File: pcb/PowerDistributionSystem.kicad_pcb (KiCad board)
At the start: 4 copper layers, 66 x 60 mm, 65 parts, among them J1 S04B-PASK-2, J2 S04B-PASK-2, J3 S04B-PASK-2, J4 S04B-PASK-2, J5 S04B-PASK-2, J8 S04B-PASK-2, U1 TPS22810DRV, U2 D24V7F5, U3 D24V7F3, U4 TMC2209-LA-T, U5 TMC2209-LA-T, U6 TMC2209-LA-T

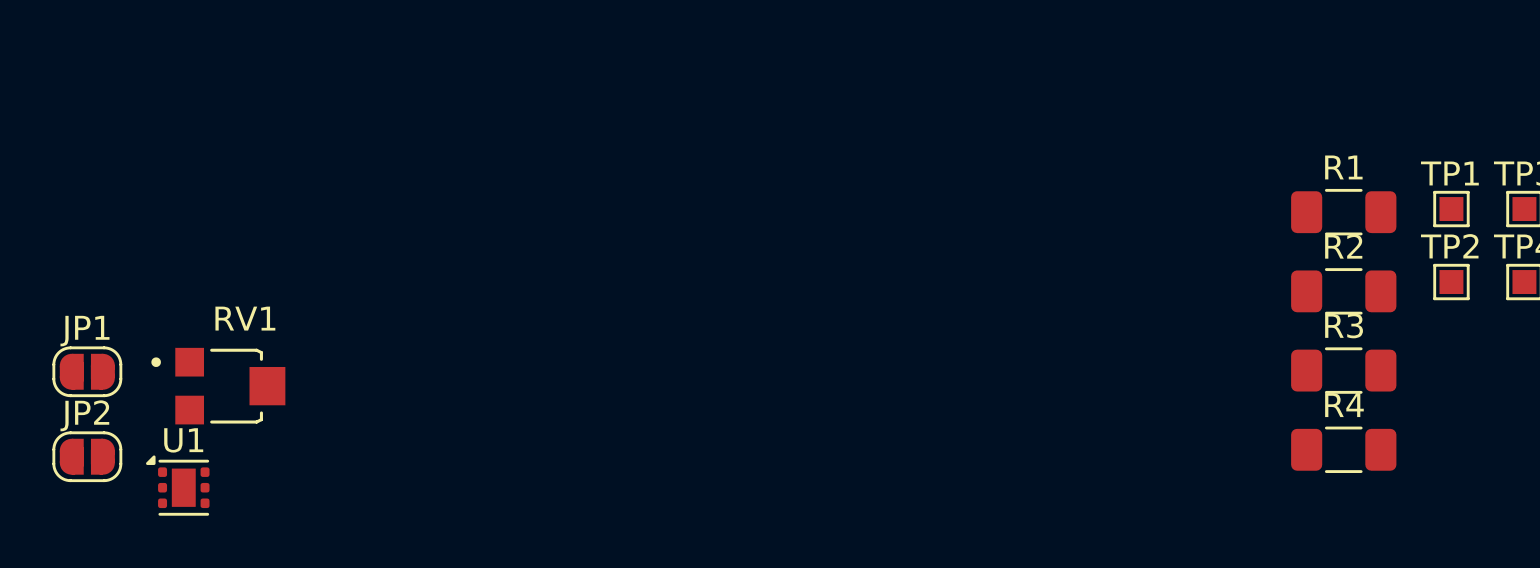
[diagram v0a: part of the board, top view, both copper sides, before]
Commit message: Removed potentiometer for VREF.
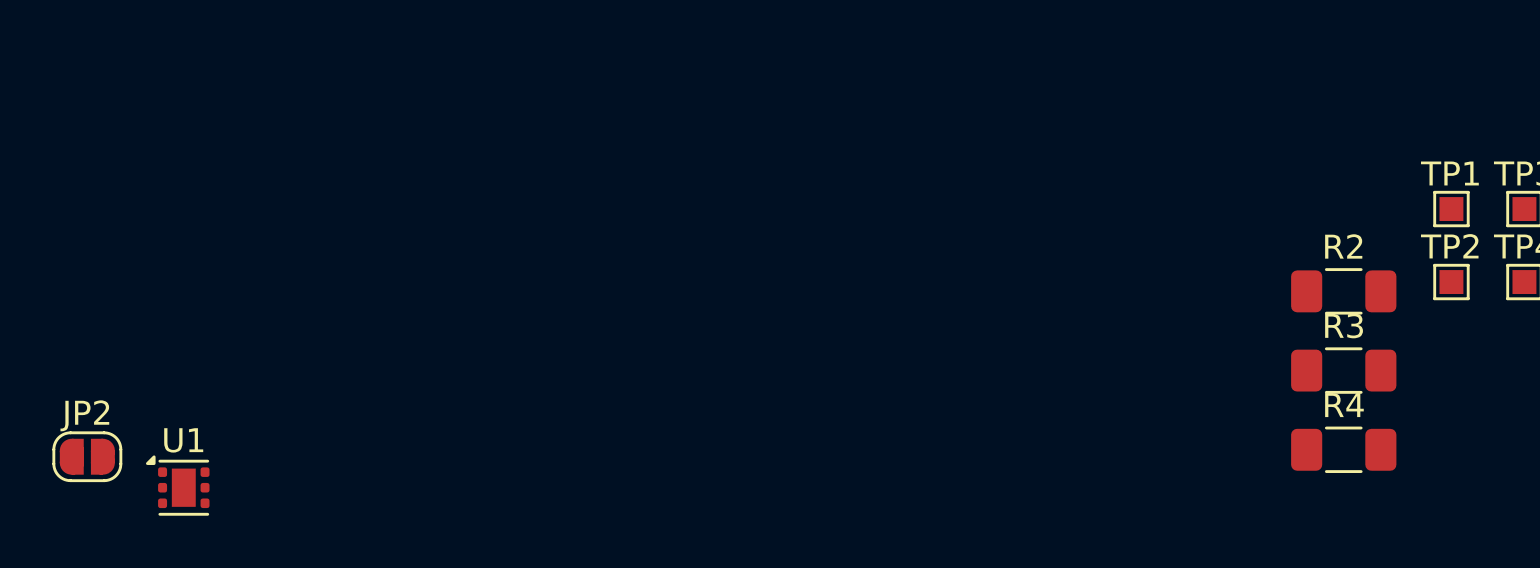
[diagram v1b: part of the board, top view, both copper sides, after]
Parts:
- removed JP1: SolderJumper_2_Open, Jumper:SolderJumper-2_P1.3mm_Open_RoundedPad1.0x1.5mm
- removed R1: 33k, Resistor_SMD:R_1206_3216Metric_Pad1.30x1.75mm_HandSolder
- removed RV1: 10k, pcb:TRIM_35WR10KLFTR

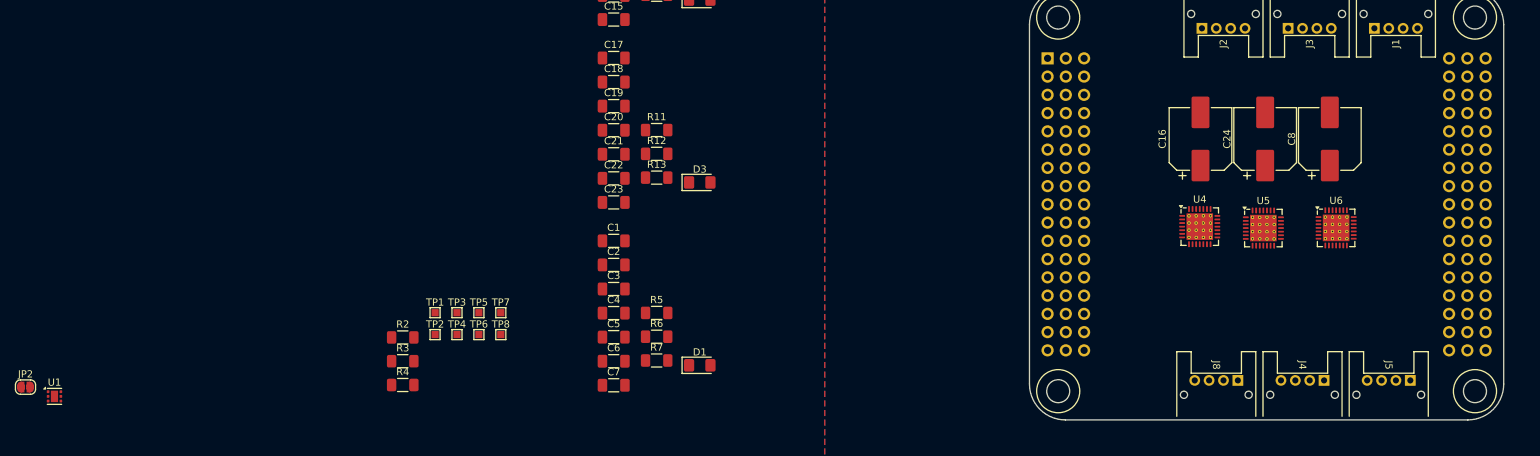
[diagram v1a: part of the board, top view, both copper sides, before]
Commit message: Updated footprints for stack connector's new asymmetry.
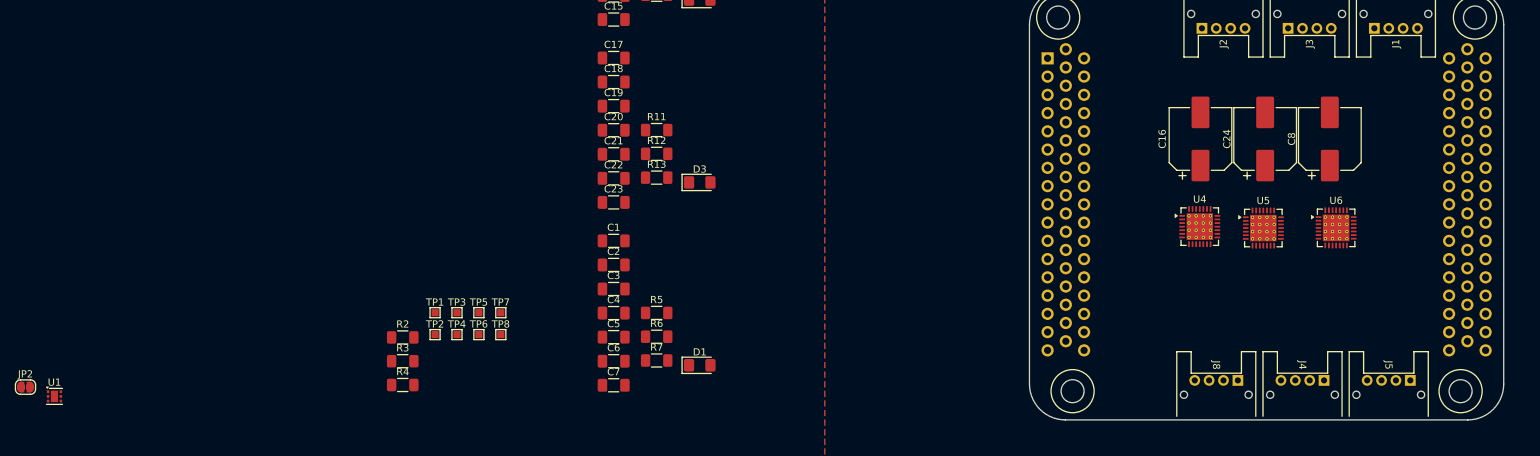
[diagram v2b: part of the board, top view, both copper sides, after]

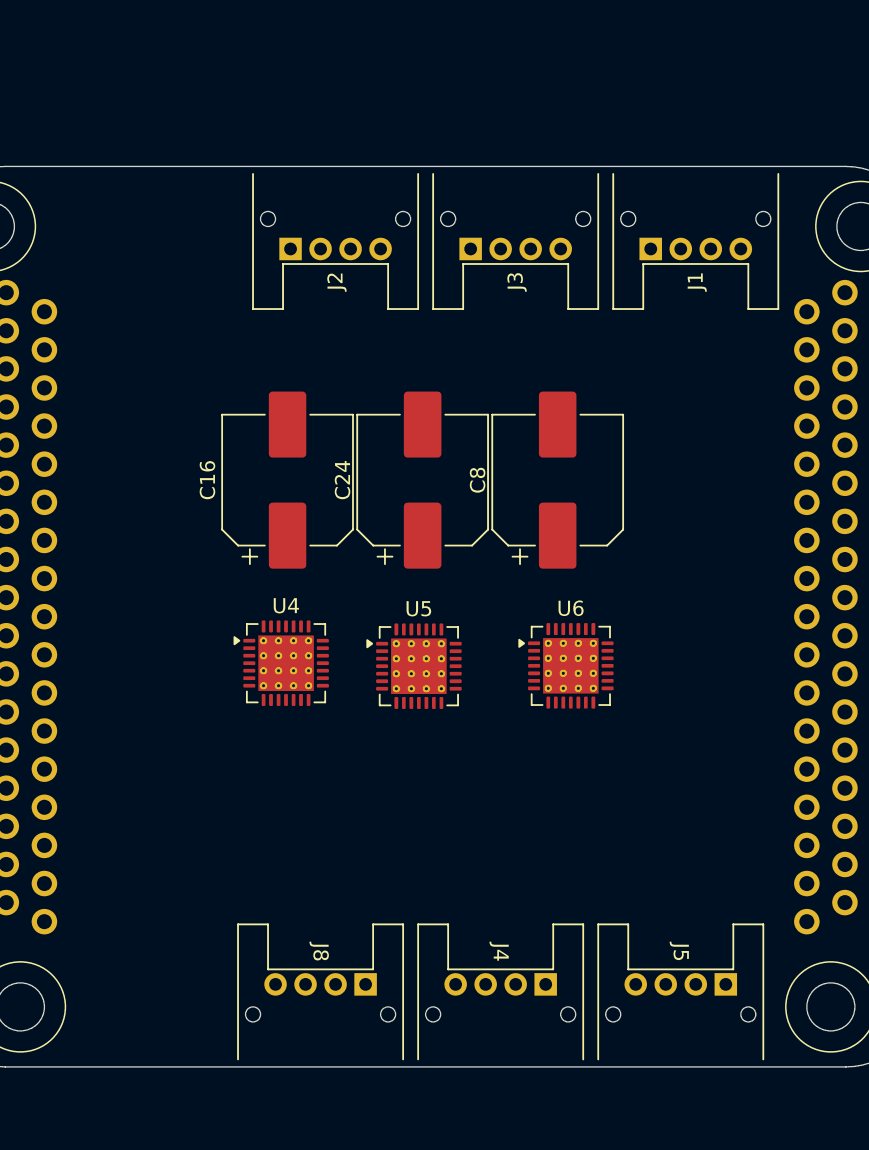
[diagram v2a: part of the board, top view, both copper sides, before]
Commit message: Instead of S04B-PASK-2 connectors, regular 2.54mm horizontal pin headers will be used.
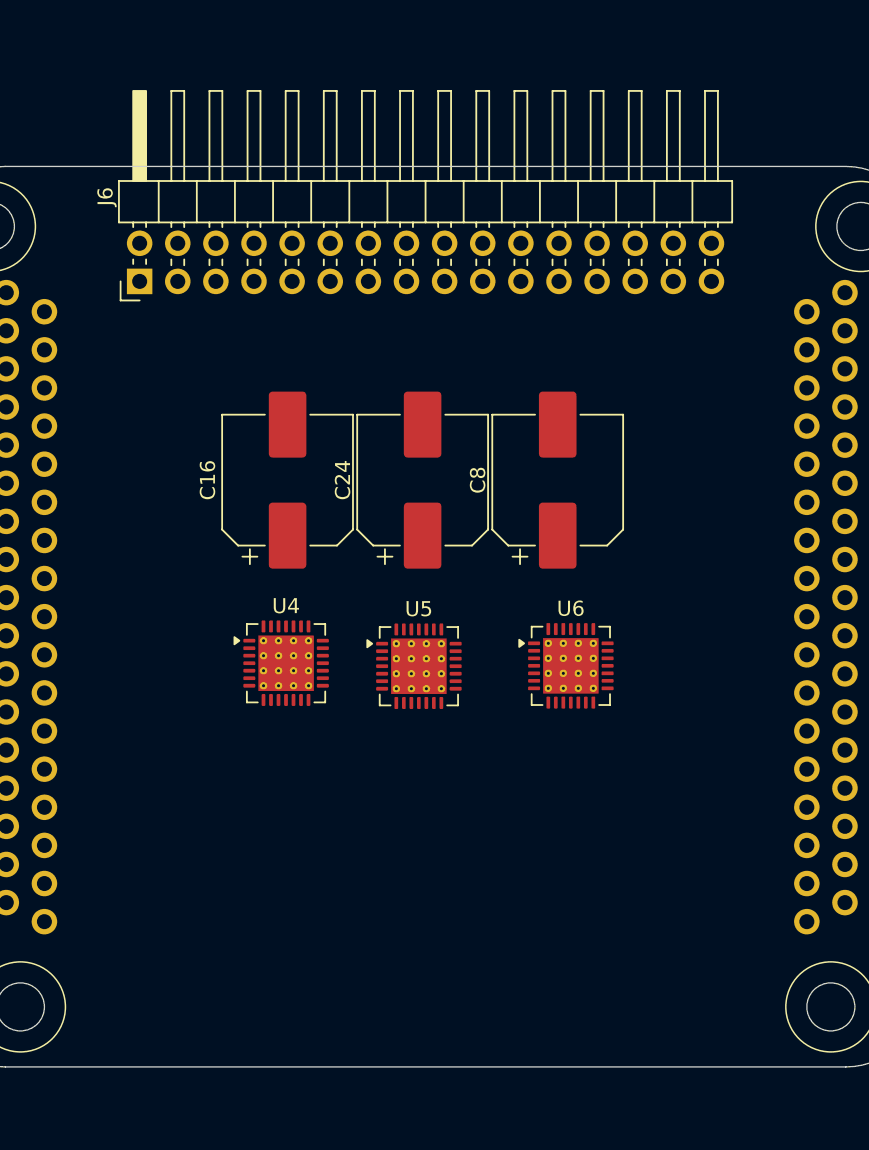
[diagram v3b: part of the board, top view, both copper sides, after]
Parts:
- removed J1, J2, J3, J4, J5, J8: S04B-PASK-2, pcb:S04B-PASK-2
- added J6: Conn_02x08_Odd_Even, Connector_PinHeader_2.54mm:PinHeader_2x16_P2.54mm_Horizontal, F.Cu at (130.9, 77.7)

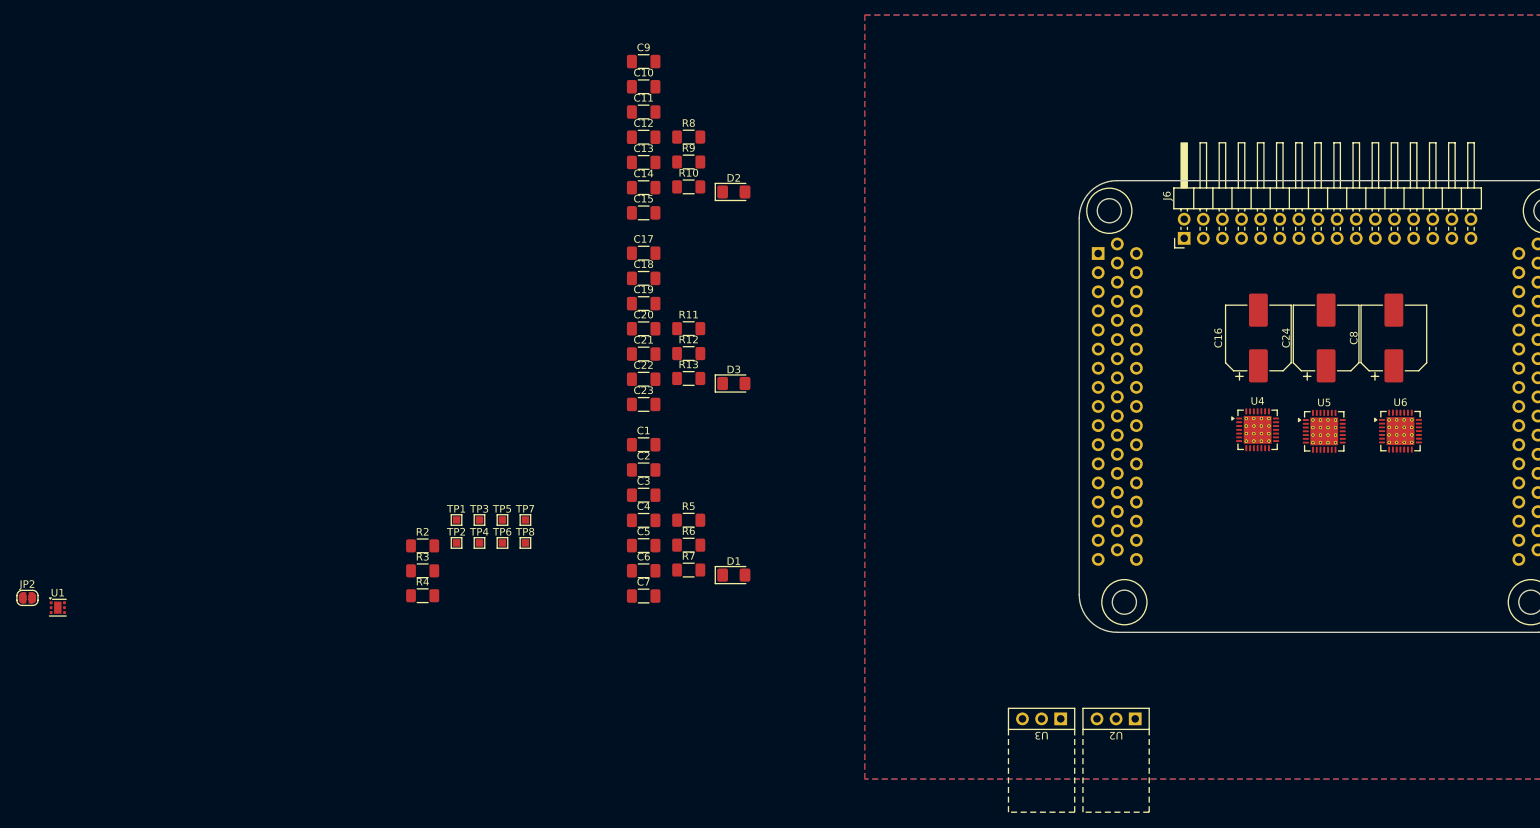
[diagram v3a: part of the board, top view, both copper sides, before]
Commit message: Laid TMC2209 stepper motor drivers out.
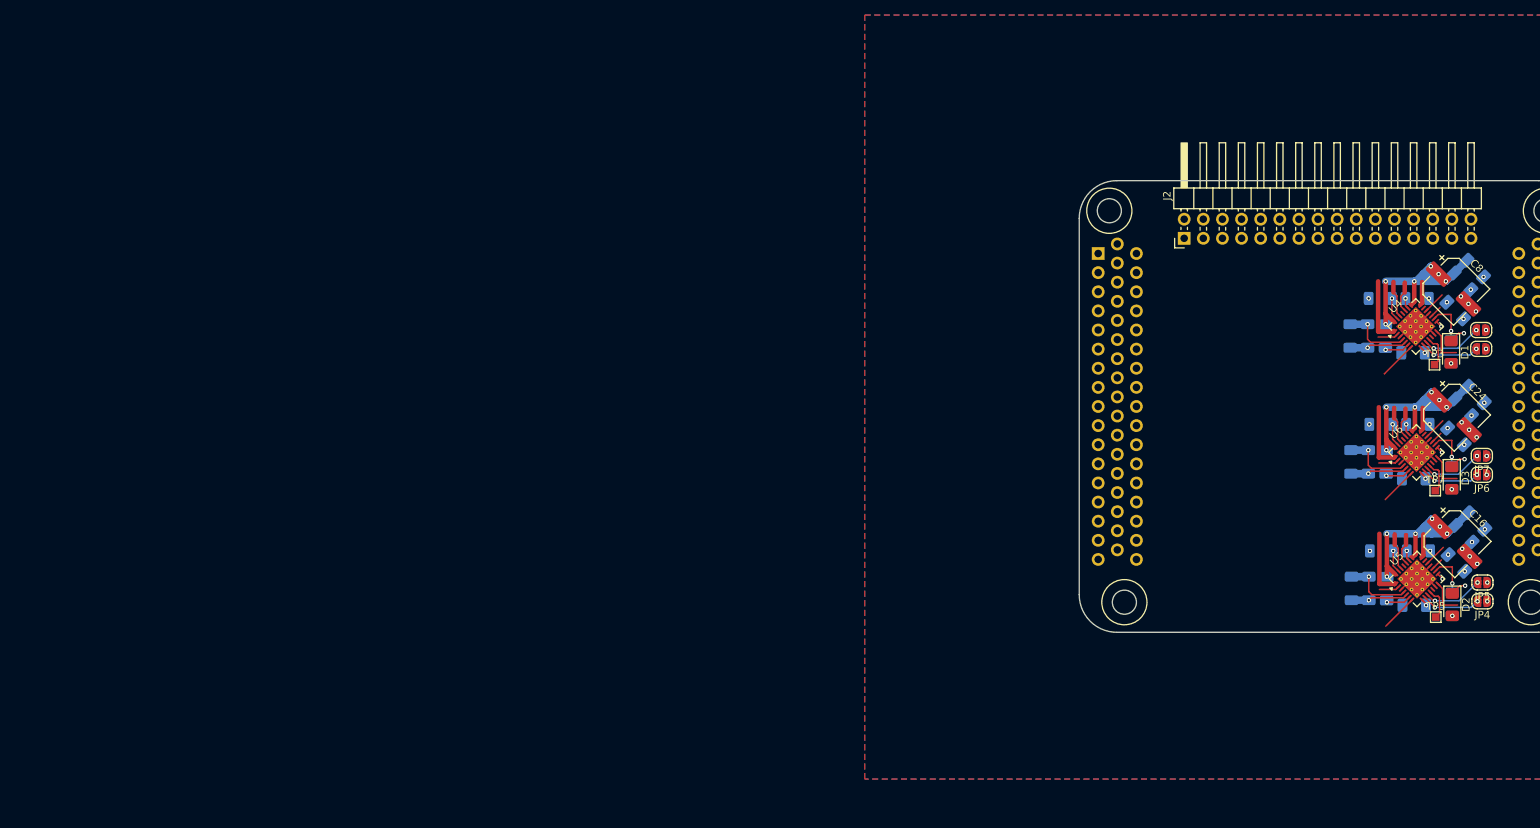
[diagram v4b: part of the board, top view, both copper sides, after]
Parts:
- removed J6: Conn_02x08_Odd_Even, Connector_PinHeader_2.54mm:PinHeader_2x16_P2.54mm_Horizontal
- removed J7: ~, pcb:StackConnector
- removed R13: RL1206FR-070R05L, Resistor_SMD:R_1206_3216Metric_Pad1.30x1.75mm_HandSolder
- removed R2: 1k, Resistor_SMD:R_1206_3216Metric_Pad1.30x1.75mm_HandSolder
- removed R3: 20k, Resistor_SMD:R_1206_3216Metric_Pad1.30x1.75mm_HandSolder
- removed TP1, TP2, TP4, TP6, TP8: TestPoint, TestPoint:TestPoint_Pad_1.0x1.0mm
- removed U1: TPS22810DRV, Package_SON:WSON-6-1EP_2x2mm_P0.65mm_EP1x1.6mm
- removed U2: D24V7F5, pcb:D24V7Fx
- removed U3: D24V7F3, pcb:D24V7Fx
- added J1: ~, pcb:StackConnector, F.Cu at (150.0, 100.0)
- added J2: PREC040DBAN-M71RC, Connector_PinHeader_2.54mm:PinHeader_2x16_P2.54mm_Horizontal, F.Cu at (130.9, 77.7)
- added JP3: SolderJumper_2_Open, Jumper:SolderJumper-2_P1.3mm_Open_RoundedPad1.0x1.5mm, F.Cu at (170.4, 89.8)
- added JP4: SolderJumper_2_Open, Jumper:SolderJumper-2_P1.3mm_Open_RoundedPad1.0x1.5mm, F.Cu at (170.6, 125.9)
- added JP5: SolderJumper_2_Open, Jumper:SolderJumper-2_P1.3mm_Open_RoundedPad1.0x1.5mm, F.Cu at (170.6, 123.4)
- added JP6: SolderJumper_2_Open, Jumper:SolderJumper-2_P1.3mm_Open_RoundedPad1.0x1.5mm, F.Cu at (170.5, 109.1)
- added JP7: SolderJumper_2_Open, Jumper:SolderJumper-2_P1.3mm_Open_RoundedPad1.0x1.5mm, F.Cu at (170.5, 106.6)
- C1, C10, C11, C12, C13, C14, C15, C17, C18, C19, C2, C20, C21, C22, C23, C3, C4, C5, C6, C7, C9, R12, R6, R9: moved to B.Cu
- C16, C24, C8: value 25TGV100M8X10.5 -> 865080343009; footprint Capacitor_SMD:CP_Elec_8x10.5 -> Capacitor_SMD:CP_Elec_6.3x5.4
- R10, R7: value RL1206FR-070R05L -> 2k; moved to B.Cu
- R11, R5, R8: value 2k -> RL1206FR-070R05L; moved to B.Cu
- R4: value 20k -> 2k; moved to B.Cu
- U4, U5, U6: footprint Package_DFN_QFN:VQFN-28-1EP_5x5mm_P0.5mm_EP3.7x3.7mm_ThermalVias -> pcb:VQFN-28-1EP_5x5mm_P0.5mm_EP3.7x3.7mm_ThermalVias
- moved JP2 195.9 mm to (170.4, 92.3), turned to 180 degrees
- moved R4 140.4 mm to (166.4, 92.7), turned to 90 degrees
- moved TP3 128.5 mm to (164.2, 94.4)
- moved C9 126.9 mm to (167.1, 120.8), turned to -45 degrees
- moved TP5 124.7 mm to (164.4, 128.0)
- moved TP7 120.9 mm to (164.3, 111.2)
- moved C12 119.8 mm to (161.5, 126.4), turned to 180 degrees
- moved C10 119.1 mm to (157.8, 124.2), turned to -90 degrees
- moved C7 118.7 mm to (169.6, 81.7), turned to -45 degrees
- moved C14 118.2 mm to (168.1, 116.9), turned to -45 degrees
- moved C15 118.0 mm to (169.8, 115.2), turned to -45 degrees
- moved C6 115.4 mm to (167.9, 83.4), turned to -45 degrees
- moved C11 115.3 mm to (155.5, 124.2), turned to -90 degrees
- moved C17 110.6 mm to (167.0, 104.0), turned to -45 degrees
- moved C23 110.6 mm to (169.7, 98.4), turned to -45 degrees
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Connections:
- net /Stepper Motor Driver - X/5VOUT renamed Net-(U4-5VOUT)
- net /Stepper Motor Driver - X/CPI renamed Net-(U4-CPI)
- net /Stepper Motor Driver - X/CPO renamed Net-(U4-CPO)
- net /Stepper Motor Driver - X/DIAGNOSTIC renamed Net-(U4-DIAG)
- net /Stepper Motor Driver - X/UART renamed MOTOR_UART_RX
- net /Stepper Motor Driver - Y/5VOUT renamed Net-(U5-5VOUT)
- net /Stepper Motor Driver - Y/CPI renamed Net-(U5-CPI)
- net /Stepper Motor Driver - Y/CPO renamed Net-(U5-CPO)
- net /Stepper Motor Driver - Y/DIAGNOSTIC renamed Net-(U5-DIAG)
- net /Stepper Motor Driver - Z/5VOUT renamed Net-(U6-5VOUT)
- net /Stepper Motor Driver - Z/CPI renamed Net-(U6-CPI)
- net /Stepper Motor Driver - Z/CPO renamed Net-(U6-CPO)
- net /Stepper Motor Driver - Z/DIAGNOSTIC renamed Net-(U6-DIAG)
- D1 pad 2: /Stepper Motor Driver - X/MOTOR_DRIVER_STEP_LED_ANODE -> Net-(D1-A)
- D2 pad 2: /Stepper Motor Driver - Y/MOTOR_DRIVER_STEP_LED_ANODE -> Net-(D2-A)
- D3 pad 2: /Stepper Motor Driver - Z/MOTOR_DRIVER_STEP_LED_ANODE -> Net-(D3-A)
- JP2 pad 2: /Stepper Motor Driver - X/SPREAD -> Net-(JP2-B)
- R10 pad 1: GND -> Net-(D3-A)
- R10 pad 2: /Stepper Motor Driver - Y/BRA -> MOTOR_STEP_Z
- R11 pad 1: /Stepper Motor Driver - Z/MOTOR_DRIVER_STEP_LED_ANODE -> GND
- R11 pad 2: MOTOR_STEP_Z -> Net-(U6-BRB)
- R12 pad 2: /Stepper Motor Driver - Z/BRB -> Net-(U6-BRA)
- R4 pad 1: +3.3V -> Net-(D1-A)
- R4 pad 2: MOTOR_ENABLE -> MOTOR_STEP_X
- R5 pad 1: /Stepper Motor Driver - X/MOTOR_DRIVER_STEP_LED_ANODE -> GND
- R5 pad 2: MOTOR_STEP_X -> Net-(U4-BRB)
- R6 pad 2: /Stepper Motor Driver - X/BRB -> Net-(U4-BRA)
- R7 pad 1: GND -> Net-(D2-A)
- R7 pad 2: /Stepper Motor Driver - X/BRA -> MOTOR_STEP_Y
- R8 pad 1: /Stepper Motor Driver - Y/MOTOR_DRIVER_STEP_LED_ANODE -> GND
- R8 pad 2: MOTOR_STEP_Y -> Net-(U5-BRB)
- R9 pad 2: /Stepper Motor Driver - Y/BRB -> Net-(U5-BRA)
- U4 pad 10: MOTOR_MICROSTEP_2_X -> Net-(JP3-B)
- U4 pad 12: /Stepper Motor Driver - X/INDEX -> unconnected-(U4-INDEX-Pad12)
- U4 pad 2: MOTOR_ENABLE -> /Stepper Motor Driver - X/DISABLE
- U4 pad 23: /Stepper Motor Driver - X/BRA -> Net-(U4-BRA)
- U4 pad 25: GND -> unconnected-(U4-NC-Pad25)
- U4 pad 27: /Stepper Motor Driver - X/BRB -> Net-(U4-BRB)
- U4 pad 9: MOTOR_MICROSTEP_1_X -> Net-(JP2-B)
- U5 pad 10: MOTOR_MICROSTEP_2_Y -> Net-(JP5-B)
- U5 pad 12: /Stepper Motor Driver - Y/INDEX -> unconnected-(U5-INDEX-Pad12)
- U5 pad 2: MOTOR_ENABLE -> /Stepper Motor Driver - X/DISABLE
- U5 pad 23: /Stepper Motor Driver - Y/BRA -> Net-(U5-BRA)
- U5 pad 25: GND -> unconnected-(U5-NC-Pad25)
- U5 pad 27: /Stepper Motor Driver - Y/BRB -> Net-(U5-BRB)
- U5 pad 9: MOTOR_MICROSTEP_1_Y -> Net-(JP4-B)
- U6 pad 10: MOTOR_MICROSTEP_2_Z -> Net-(JP7-B)
- U6 pad 12: /Stepper Motor Driver - Z/INDEX -> unconnected-(U6-INDEX-Pad12)
- U6 pad 2: MOTOR_ENABLE -> /Stepper Motor Driver - X/DISABLE
- U6 pad 23: /Stepper Motor Driver - Z/BRA -> Net-(U6-BRA)
- U6 pad 25: GND -> unconnected-(U6-NC-Pad25)
- U6 pad 27: /Stepper Motor Driver - Z/BRB -> Net-(U6-BRB)
- U6 pad 9: MOTOR_MICROSTEP_1_Z -> Net-(JP6-B)
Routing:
- net +MOTOR: track 0.00 -> 95.4 mm, vias 0 -> 18
- net GND: track 0.00 -> 30.3 mm, vias 0 -> 27
- net MOTOR_UART_RX: track 0.00 -> 15.1 mm
- net /Stepper Motor Driver - X/SPREAD: track 0.00 -> 14.8 mm
- net Net-(U5-CPO): track 0.00 -> 9.29 mm, vias 0 -> 1
- net Net-(U6-CPO): track 0.00 -> 9.29 mm, vias 0 -> 1
- net Net-(U4-CPO): track 0.00 -> 9.29 mm, vias 0 -> 1
- net MOTOR_DRIVER_B2_Y: track 0.00 -> 8.83 mm
- net MOTOR_DRIVER_B2_X: track 0.00 -> 8.83 mm
- net MOTOR_DRIVER_B2_Z: track 0.00 -> 8.83 mm
- net /Stepper Motor Driver - X/DISABLE: track 0.00 -> 8.19 mm
- net Net-(JP3-B): track 0.00 -> 8.00 mm, vias 0 -> 2
- net Net-(JP5-B): track 0.00 -> 8.00 mm, vias 0 -> 2
- net Net-(JP7-B): track 0.00 -> 8.00 mm, vias 0 -> 2
- net Net-(JP2-B): track 0.00 -> 7.91 mm, vias 0 -> 2
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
